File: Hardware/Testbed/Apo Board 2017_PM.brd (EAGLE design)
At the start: 96.5 x 62.2 mm, 5 parts

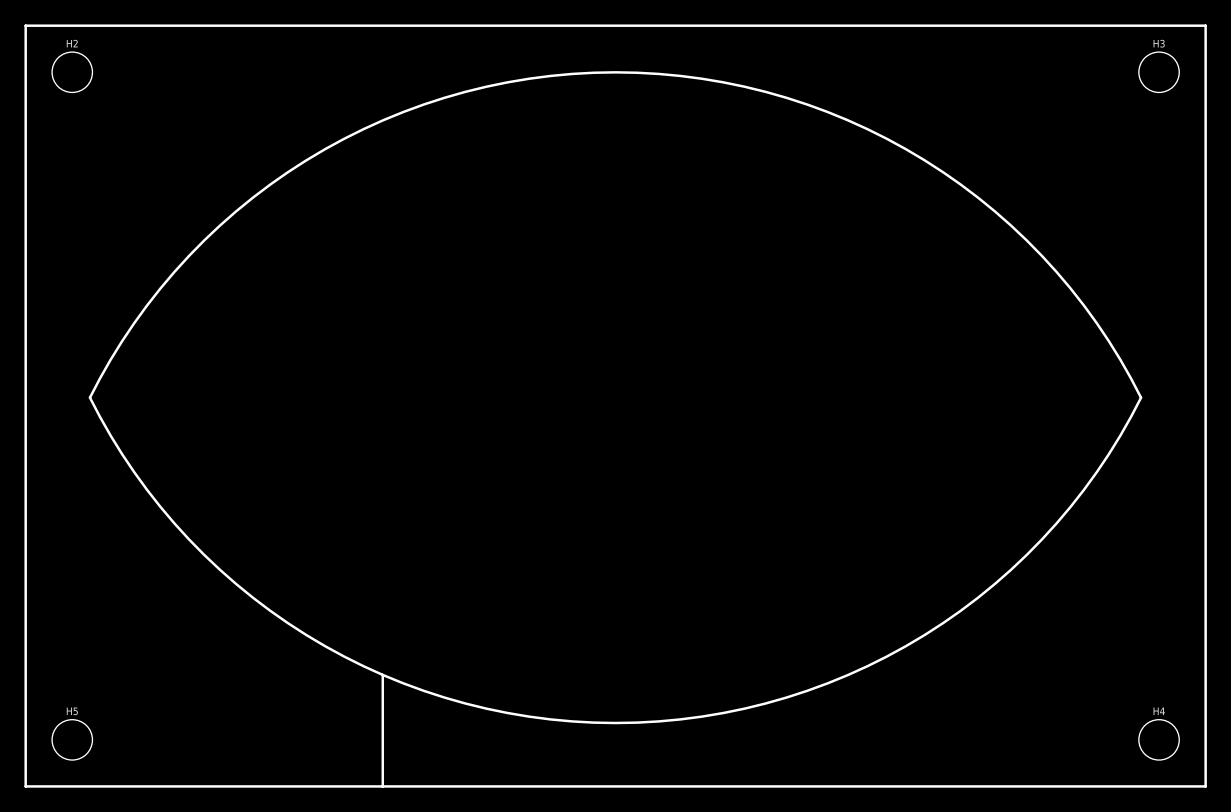
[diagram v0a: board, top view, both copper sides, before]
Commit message: Pogo Bed finished.
Finished making pogoed programming and testing fixture. Moving to
Hardware Folder
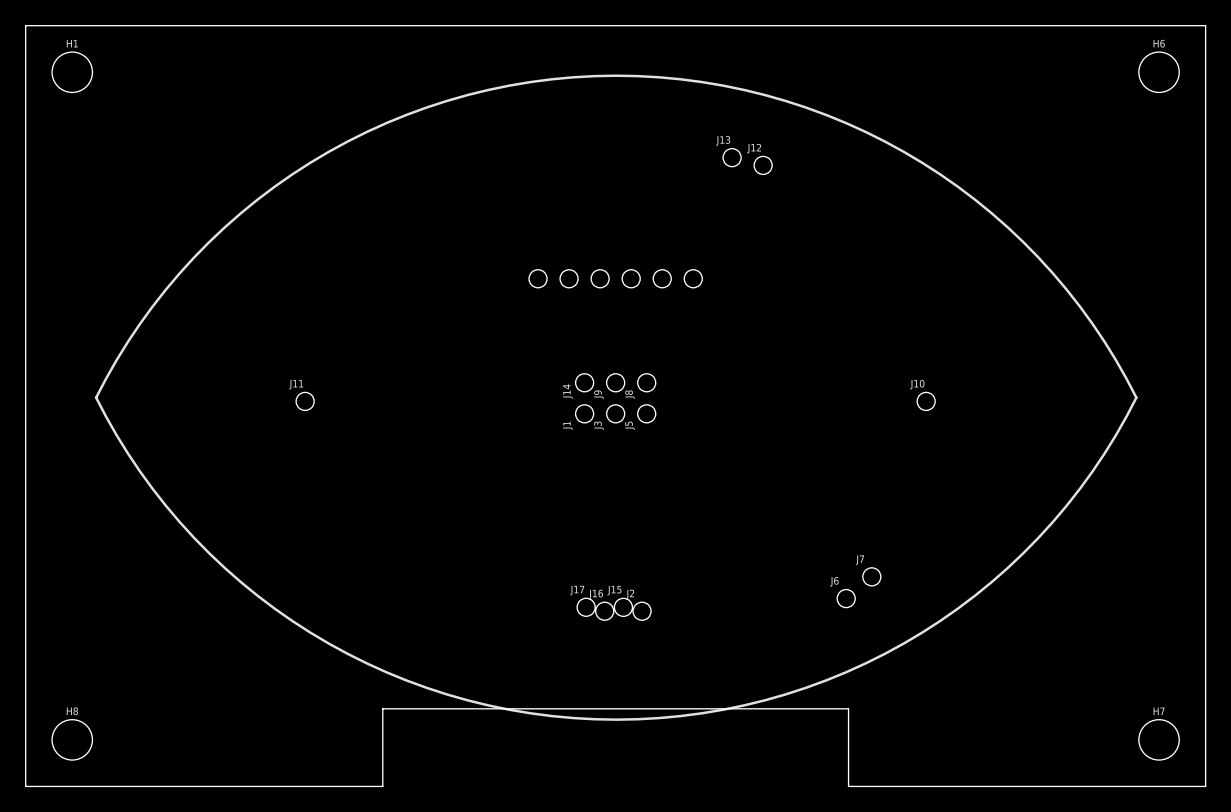
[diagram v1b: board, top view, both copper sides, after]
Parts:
- added J1, J10, J11, J12, J13, J14, J15, J16, J17, J2, J3, J5, J6, J7, J8, J9: (no value), SparkFun-Connectors:1X01_POGOPIN_HOLE_0.58_DIA
- added J4: (no value), SparkFun-Connectors:1X06_HOLES_ONLY
- renumbered H2 to H1, H3 to H6, H4 to H7, H5 to H8
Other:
- outline, holes or cut-outs redrawn
- board text added: "5V"
- board text added: "A4"
- board text added: "A5"
- board text added: "DTR"
- board text added: "GND"
- board text added: "MISO"
- board text added: "RST"
- board text added: "RX"
- board text added: "SCK"
- board text added: "SCL"
- board text added: "SDA"
- board text added: "TX"
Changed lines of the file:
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@@
 <board>
 <plain>
-<wire x1="-42.4942" y1="0.0508" x2="42.5958" y2="0.0508" width="0.2032" layer="51" curve="-127.037923"/>
-<wire x1="42.5958" y1="0.0508" x2="-42.4942" y2="0.0508" width="0.2032" layer="51" curve="-127.037923"/>
+<wire x1="-42.4942" y1="0.0508" x2="42.5958" y2="0.0508" width="0.2032" layer="21" curve="-127.037923"/>
+<wire x1="42.5958" y1="0.0508" x2="-42.4942" y2="0.0508" width="0.2032" layer="21" curve="-127.037923"/>
 <text x="4.826" y="-39.751" size="1.778" layer="27" font="vector" ratio="10">Joel Bartlett</text>
-<wire x1="-48.26" y1="30.48" x2="48.26" y2="30.48" width="0.2032" layer="20"/>
-<wire x1="48.26" y1="30.48" x2="48.26" y2="-31.75" width="0.2032" layer="20"/>
-<wire x1="48.26" y1="-31.75" x2="-19.05" y2="-31.75" width="0.2032" layer="20"/>
-<wire x1="-19.05" y1="-31.75" x2="-48.26" y2="-31.75" width="0.2032" layer="20"/>
-<wire x1="-48.26" y1="-31.75" x2="-48.26" y2="30.48" width="0.2032" layer="20"/>
-<wire x1="-43.0022" y1="0.0508" x2="42.9768" y2="0.0508" width="0.2032" layer="20" curve="-127.037923"/>
-<wire x1="42.9768" y1="0.0508" x2="-43.0022" y2="0.0508" width="0.2032" layer="20" curve="-127.037923"/>
-<wire x1="-19.05" y1="-31.75" x2="-19.05" y2="-22.62378125" width="0.2032" layer="20"/>
+<circle x="-2.54" y="1.27" radius="1.27" width="0.4064" layer="51"/>
+<circle x="0" y="1.27" radius="1.27" width="0.4064" layer="51"/>
+<circle x="2.54" y="1.27" radius="1.27" width="0.4064" layer="51"/>
+<circle x="2.54" y="-1.27" radius="1.27" width="0.4064" layer="51"/>
+<circle x="0" y="-1.27" radius="1.27" width="0.4064" layer="51"/>
+<circle x="-2.54" y="-1.27" radius="1.27" width="0.4064" layer="51"/>
+<text x="-3.048" y="6.35" size="0.9398" layer="51" font="vector" ratio="15" rot="MR90" align="bottom-right">MISO</text>
+<text x="-0.508" y="5.461" size="0.9398" layer="51" font="vector" ratio="15" rot="MR90" align="bottom-right">SCK</text>
+<text x="2.032" y="5.461" size="0.9398" layer="51" font="vector" ratio="15" rot="MR90" align="bottom-right">RST</text>
+<text x="0.635" y="13.208" size="0.9398" layer="51" font="vector" ratio="15" rot="MR90" align="bottom-right">5V</text>
+<text x="-4.3815" y="13.2715" size="0.9398" layer="51" font="vector" ratio="15" rot="MR90" align="bottom-right">TX</text>
+<text x="-1.8415" y="13.2715" size="0.9398" layer="51" font="vector" ratio="15" rot="MR90" align="bottom-right">RX</text>
+<text x="-6.858" y="11.557" size="0.9398" layer="51" font="vector" ratio="15" rot="MR90">DTR</text>
+<text x="3.302" y="13.843" size="0.9398" layer="51" font="vector" ratio="15" rot="MR90" align="bottom-right">GND</text>
+<text x="5.842" y="13.843" size="0.9398" layer="51" font="vector" ratio="15" rot="MR90" align="bottom-right">GND</text>
+<text x="15.113" y="15.621" size="0.9398" layer="51" font="vector" ratio="15" rot="MR270" align="bottom-right">A4</text>
+<text x="12.573" y="16.256" size="0.9398" layer="51" font="vector" ratio="15" rot="MR270" align="bottom-right">A5</text>
+<circle x="17.145" y="17.78" radius="0.635" width="0.254" layer="51"/>
+<circle x="14.605" y="18.415" radius="0.635" width="0.254" layer="51"/>
+<circle x="12.065" y="19.05" radius="0.635" width="0.254" layer="51"/>
+<circle x="9.525" y="19.685" radius="0.635" width="0.254" layer="51"/>
+<circle x="-25.4" y="-0.254" radius="0.803215625" width="0.254" layer="51"/>
+<circle x="25.4" y="-0.254" radius="0.772509375" width="0.254" layer="51"/>
+<circle x="-6.35" y="9.7155" radius="1.08694375" width="0.254" layer="51"/>
+<circle x="-3.81" y="9.7155" radius="1.08694375" width="0.254" layer="51"/>
+<circle x="-1.27" y="9.7155" radius="1.08694375" width="0.254" layer="51"/>
+<circle x="1.27" y="9.7155" radius="1.08694375" width="0.254" layer="51"/>
+<circle x="3.81" y="9.7155" radius="1.08694375" width="0.254" layer="51"/>
+<circle x="6.35" y="9.7155" radius="1.08694375" width="0.254" layer="51"/>
+<circle x="-2.54" y="1.27" radius="0.635" width="0.254" layer="51"/>
+<circle x="0" y="1.27" radius="0.635" width="0.254" layer="51"/>
+<circle x="2.54" y="1.27" radius="0.635" width="0.254" layer="51"/>
+<circle x="2.54" y="-1.27" radius="0.635" width="0.254" layer="51"/>
+<circle x="0" y="-1.27" radius="0.635" width="0.254" layer="51"/>
+<circle x="-2.54" y="-1.27" radius="0.635" width="0.254" layer="51"/>
+<text x="17.653" y="18.796" size="0.9398" layer="51" font="vector" ratio="15" rot="MR270" align="bottom-right">GND</text>
+<text x="15.113" y="19.431" size="0.9398" layer="51" font="vector" ratio="15" rot="MR270" align="bottom-right">SDA</text>
+<text x="12.573" y="20.066" size="0.9398" layer="51" font="vector" ratio="15" rot="MR270" align="bottom-right">SCL</text>
+<text x="9.017" y="22.352" size="0.9398" layer="51" font="vector" ratio="15" rot="MR90" align="bottom-right">5V</text>
+<circle x="18.8722" y="-16.3576" radius="1.1447625" width="0.254" layer="51"/>
+<circle x="20.96135" y="-14.61135" radius="1.1447625" width="0.254" layer="51"/>
+<wire x1="-26.035" y1="2.54" x2="-24.765" y2="2.54" width="0.254" layer="51"/>
+<wire x1="24.765" y1="2.54" x2="26.035" y2="2.54" width="0.254" layer="51"/>
+<wire x1="25.4" y1="3.175" x2="25.4" y2="1.905" width="0.254" layer="51"/>
+<wire x1="-48.26" y1="30.48" x2="48.26" y2="30.48" width="0" layer="20"/>
+<wire x1="48.26" y1="30.48" x2="48.26" y2="-31.75" width="0" layer="20"/>
+<wire x1="48.26" y1="-31.75" x2="19.05" y2="-31.75" width="0" layer="20"/>
+<wire x1="-19.05" y1="-31.75" x2="-48.26" y2="-31.75" width="0" layer="20"/>
+<wire x1="-48.26" y1="-31.75" x2="-48.26" y2="30.48" width="0" layer="20"/>
+<wire x1="19.05" y1="-25.4" x2="19.05" y2="-31.75" width="0" layer="20"/>
+<wire x1="-19.05" y1="-31.75" x2="-19.05" y2="-25.4" width="0" layer="20"/>
+<wire x1="-19.05" y1="-25.4" x2="19.05" y2="-25.4" width="0" layer="20"/>
+<circle x="-2.413" y="-17.0942" radius="0.568278125" width="0.254" layer="51"/>
+<circle x="0.635" y="-17.10055" radius="0.568278125" width="0.254" layer="51"/>
+<circle x="-0.89535" y="-17.41805" radius="0.568278125" width="0.254" layer="51"/>
+<circle x="2.159" y="-17.41805" radius="0.568278125" width="0.254" layer="51"/>
 </plain>
 <attributes>
@@
 </autorouter>
 <elements>
-<element name="H2" library="SparkFun-Hardware" package="STAND-OFF" value="STAND-OFF" x="-44.45" y="26.67"/>
-<element name="H3" library="SparkFun-Hardware" package="STAND-OFF" value="STAND-OFF" x="44.45" y="26.67"/>
-<element name="H4" library="SparkFun-Hardware" package="STAND-OFF" value="STAND-OFF" x="44.45" y="-27.94"/>
-<element name="H5" library="SparkFun-Hardware" package="STAND-OFF" value="STAND-OFF" x="-44.45" y="-27.94"/>
+<element name="J4" library="SparkFun-Connectors" package="1X06_HOLES_ONLY" value="" x="-6.35" y="9.779">
+<attribute name="PROD_ID" value="CONN-08437" x="-6.35" y="9.779" size="1.778" layer="27" display="off"/>
+</element>
+<element name="J6" library="SparkFun-Connectors" package="1X01_POGOPIN_HOLE_0.58_DIA" value="" x="18.8595" y="-16.383"/>
+<element name="J7" library="SparkFun-Connectors" package="1X01_POGOPIN_HOLE_0.58_DIA" value="" x="20.955" y="-14.605"/>
+<element name="J10" library="SparkFun-Connectors" package="1X01_POGOPIN_HOLE_0.58_DIA" value="" x="25.4" y="-0.254"/>
+<element name="J11" library="SparkFun-Connectors" package="1X01_POGOPIN_HOLE_0.58_DIA" value="" x="-25.4" y="-0.254"/>
+<element name="J12" library="SparkFun-Connectors" package="1X01_POGOPIN_HOLE_0.58_DIA" value="" x="12.065" y="19.05"/>
+<element name="J13" library="SparkFun-Connectors" package="1X01_POGOPIN_HOLE_0.58_DIA" value="" x="9.525" y="19.685"/>
 <element name="FRAME1" library="SparkFun-Aesthetics" package="CREATIVE_COMMONS" value="FRAME-LETTER" x="-26.67" y="-48.26"/>
+<element name="J1" library="SparkFun-Connectors" package="1X01_POGOPIN_HOLE_0.58_DIA" value="" x="-2.54" y="-1.27" rot="R90"/>
+<element name="J3" library="SparkFun-Connectors" package="1X01_POGOPIN_HOLE_0.58_DIA" value="" x="0" y="-1.27" rot="R90"/>
+<element name="J5" library="SparkFun-Connectors" package="1X01_POGOPIN_HOLE_0.58_DIA" value="" x="2.54" y="-1.27" rot="R90"/>
+<element name="J8" library="SparkFun-Connectors" package="1X01_POGOPIN_HOLE_0.58_DIA" value="" x="2.54" y="1.27" rot="R90"/>
+<element name="J9" library="SparkFun-Connectors" package="1X01_POGOPIN_HOLE_0.58_DIA" value="" x="0" y="1.27" rot="R90"/>
+<element name="J14" library="SparkFun-Connectors" package="1X01_POGOPIN_HOLE_0.58_DIA" value="" x="-2.54" y="1.27" rot="R90"/>
+<element name="H1" library="SparkFun-Hardware" package="STAND-OFF" value="STAND-OFF" x="-44.45" y="26.67"/>
+<element name="H6" library="SparkFun-Hardware" package="STAND-OFF" value="STAND-OFF" x="44.45" y="26.67"/>
+<element name="H7" library="SparkFun-Hardware" package="STAND-OFF" value="STAND-OFF" x="44.45" y="-27.94"/>
+<element name="H8" library="SparkFun-Hardware" package="STAND-OFF" value="STAND-OFF" x="-44.45" y="-27.94"/>
+<element name="J2" library="SparkFun-Connectors" package="1X01_POGOPIN_HOLE_0.58_DIA" value="" x="2.159" y="-17.41805"/>
+<element name="J15" library="SparkFun-Connectors" package="1X01_POGOPIN_HOLE_0.58_DIA" value="" x="0.635" y="-17.10055"/>
+<element name="J16" library="SparkFun-Connectors" package="1X01_POGOPIN_HOLE_0.58_DIA" value="" x="-0.89535" y="-17.41805"/>
+<element name="J17" library="SparkFun-Connectors" package="1X01_POGOPIN_HOLE_0.58_DIA" value="" x="-2.413" y="-17.0942"/>
 </elements>
 <signals>
